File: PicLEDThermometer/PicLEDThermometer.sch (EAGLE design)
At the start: 27 parts, among them IC1 74LS595N, Q1 MCP1702-3302E/TO, Q2 2N2222TO92, Q3 2N2222TO92, Q4 2N2222TO92, Q5 2N2222TO92

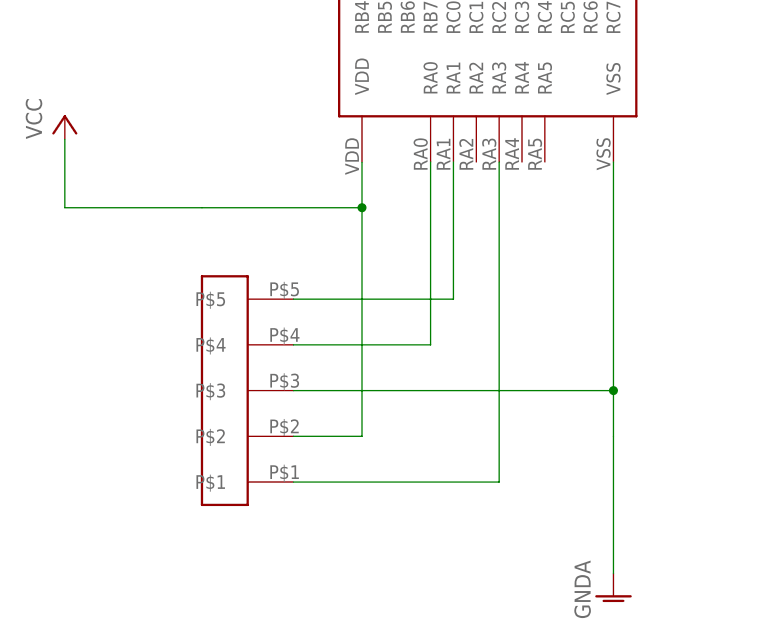
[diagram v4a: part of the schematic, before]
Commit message: Change ICSP header to standard pin header. Add the ICSP resistor.
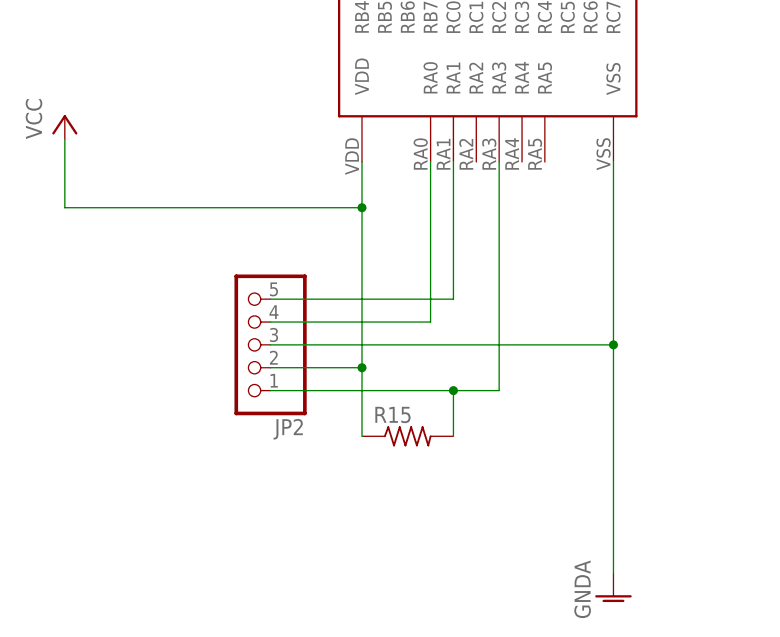
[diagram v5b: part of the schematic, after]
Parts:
- removed U$3: JST-PH-5POS, con-JST:JST-PH-5POS
- added JP2: (no value), pinhead:PINHD-1X5
- added R15: (no value), rcl:R-US_0207/10
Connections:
- net GNDA: now also JP2.3; no longer U$3.P$3
- net N$10: now also JP2.5; no longer U$3.P$5
- net N$8: now also JP2.1, R15.2; no longer U$3.P$1
- net N$9: now also JP2.4; no longer U$3.P$4
- net VCC: now also JP2.2, R15.1; no longer U$3.P$2
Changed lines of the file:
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@@
 <part name="VDD3" library="supply1" deviceset="VDD" device=""/>
 <part name="GND7" library="supply1" library_urn="urn:adsk.eagle:library:371" deviceset="GNDA" device=""/>
-<part name="U$3" library="con-JST" deviceset="JST-PH-5POS" device=""/>
 <part name="GND4" library="supply1" library_urn="urn:adsk.eagle:library:371" deviceset="GNDA" device=""/>
 <part name="P+4" library="supply1" library_urn="urn:adsk.eagle:library:371" deviceset="VCC" device=""/>
@@
 <part name="R13" library="rcl" library_urn="urn:adsk.eagle:library:334" deviceset="R-US_" device="0207/10"/>
 <part name="R14" library="rcl" library_urn="urn:adsk.eagle:library:334" deviceset="R-US_" device="0207/10"/>
+<part name="JP2" library="pinhead" library_urn="urn:adsk.eagle:library:325" deviceset="PINHD-1X5" device="" package3d_urn="urn:adsk.eagle:package:22469/2"/>
+<part name="R15" library="rcl" library_urn="urn:adsk.eagle:library:334" deviceset="R-US_" device="0207/10"/>
 </parts>
 <sheets>
@@
 <instance part="VDD3" gate="G$1" x="114.3" y="43.18"/>
 <instance part="GND7" gate="1" x="114.3" y="25.4"/>
-<instance part="U$3" gate="G$1" x="10.16" y="-63.5" rot="R180"/>
 <instance part="GND4" gate="1" x="129.54" y="48.26"/>
 <instance part="P+4" gate="VCC" x="132.08" y="73.66"/>
@@
 <instance part="R13" gate="G$1" x="124.46" y="-20.32" rot="R270"/>
 <instance part="R14" gate="G$1" x="129.54" y="-20.32" rot="R270"/>
+<instance part="JP2" gate="A" x="12.7" y="-50.8" rot="R180"/>
+<instance part="R15" gate="G$1" x="30.48" y="-60.96"/>
 </instances>
 <busses>
@@
 <pinref part="U$2" gate="G$1" pin="VSS"/>
 <pinref part="GND2" gate="1" pin="GNDA"/>
-<wire x1="53.34" y1="-30.48" x2="53.34" y2="-55.88" width="0.1524" layer="91"/>
-<wire x1="53.34" y1="-55.88" x2="53.34" y2="-60.96" width="0.1524" layer="91"/>
-<wire x1="53.34" y1="-60.96" x2="53.34" y2="-76.2" width="0.1524" layer="91"/>
-<pinref part="U$3" gate="G$1" pin="P$3"/>
-<wire x1="17.78" y1="-55.88" x2="53.34" y2="-55.88" width="0.1524" layer="91"/>
-<junction x="53.34" y="-55.88"/>
+<wire x1="53.34" y1="-30.48" x2="53.34" y2="-50.8" width="0.1524" layer="91"/>
+<wire x1="53.34" y1="-50.8" x2="53.34" y2="-76.2" width="0.1524" layer="91"/>
+<wire x1="15.24" y1="-50.8" x2="53.34" y2="-50.8" width="0.1524" layer="91"/>
+<junction x="53.34" y="-50.8"/>
+<pinref part="JP2" gate="A" pin="3"/>
 </segment>
 <segment>
@@
 <wire x1="25.4" y1="-30.48" x2="25.4" y2="-35.56" width="0.1524" layer="91"/>
 <pinref part="P+1" gate="VCC" pin="VCC"/>
-<wire x1="25.4" y1="-35.56" x2="7.62" y2="-35.56" width="0.1524" layer="91"/>
-<wire x1="7.62" y1="-35.56" x2="-7.62" y2="-35.56" width="0.1524" layer="91"/>
+<wire x1="25.4" y1="-35.56" x2="-7.62" y2="-35.56" width="0.1524" layer="91"/>
 <wire x1="-7.62" y1="-35.56" x2="-7.62" y2="-27.94" width="0.1524" layer="91"/>
-<pinref part="U$3" gate="G$1" pin="P$2"/>
-<wire x1="17.78" y1="-60.96" x2="25.4" y2="-60.96" width="0.1524" layer="91"/>
-<wire x1="25.4" y1="-60.96" x2="25.4" y2="-35.56" width="0.1524" layer="91"/>
+<wire x1="15.24" y1="-53.34" x2="25.4" y2="-53.34" width="0.1524" layer="91"/>
+<wire x1="25.4" y1="-53.34" x2="25.4" y2="-35.56" width="0.1524" layer="91"/>
 <junction x="25.4" y="-35.56"/>
+<pinref part="JP2" gate="A" pin="2"/>
+<pinref part="R15" gate="G$1" pin="1"/>
+<wire x1="25.4" y1="-60.96" x2="25.4" y2="-53.34" width="0.1524" layer="91"/>
+<junction x="25.4" y="-53.34"/>
 </segment>
 <segment>
@@
 <segment>
 <pinref part="U$2" gate="G$1" pin="RA3"/>
-<wire x1="40.64" y1="-30.48" x2="40.64" y2="-66.04" width="0.1524" layer="91"/>
-<pinref part="U$3" gate="G$1" pin="P$1"/>
-<wire x1="40.64" y1="-66.04" x2="17.78" y2="-66.04" width="0.1524" layer="91"/>
+<wire x1="40.64" y1="-30.48" x2="40.64" y2="-55.88" width="0.1524" layer="91"/>
+<wire x1="40.64" y1="-55.88" x2="35.56" y2="-55.88" width="0.1524" layer="91"/>
+<pinref part="JP2" gate="A" pin="1"/>
+<pinref part="R15" gate="G$1" pin="2"/>
+<wire x1="35.56" y1="-55.88" x2="15.24" y2="-55.88" width="0.1524" layer="91"/>
+<wire x1="35.56" y1="-60.96" x2="35.56" y2="-55.88" width="0.1524" layer="91"/>
+<junction x="35.56" y="-55.88"/>
 </segment>
 </net>
@@
 <segment>
 <pinref part="U$2" gate="G$1" pin="RA0"/>
-<pinref part="U$3" gate="G$1" pin="P$4"/>
-<wire x1="33.02" y1="-30.48" x2="33.02" y2="-50.8" width="0.1524" layer="91"/>
-<wire x1="33.02" y1="-50.8" x2="17.78" y2="-50.8" width="0.1524" layer="91"/>
+<wire x1="33.02" y1="-30.48" x2="33.02" y2="-48.26" width="0.1524" layer="91"/>
+<wire x1="33.02" y1="-48.26" x2="15.24" y2="-48.26" width="0.1524" layer="91"/>
+<pinref part="JP2" gate="A" pin="4"/>
 </segment>
 </net>
@@
 <segment>
 <pinref part="U$2" gate="G$1" pin="RA1"/>
-<pinref part="U$3" gate="G$1" pin="P$5"/>
 <wire x1="35.56" y1="-30.48" x2="35.56" y2="-45.72" width="0.1524" layer="91"/>
-<wire x1="35.56" y1="-45.72" x2="17.78" y2="-45.72" width="0.1524" layer="91"/>
-</segment>
-</net>
+<wire x1="35.56" y1="-45.72" x2="15.24" y2="-45.72" width="0.1524" layer="91"/>
+<pinref part="JP2" gate="A" pin="5"/>
+</segment>
+</net>
